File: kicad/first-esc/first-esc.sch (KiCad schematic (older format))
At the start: 0 parts

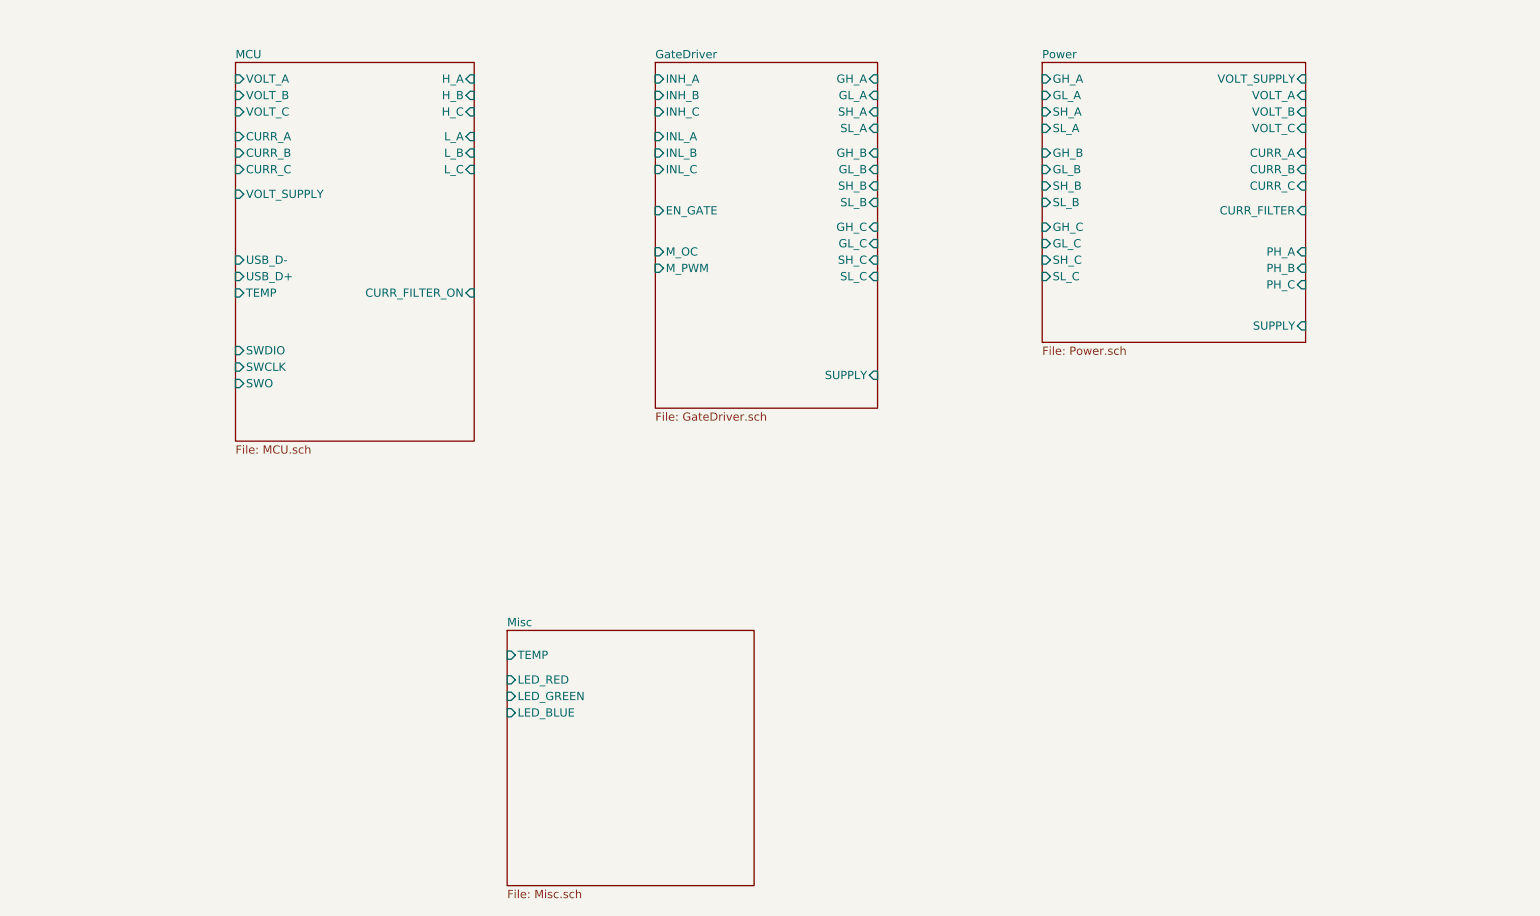
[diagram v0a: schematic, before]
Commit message: (hopefully) finishing up PCB schematic
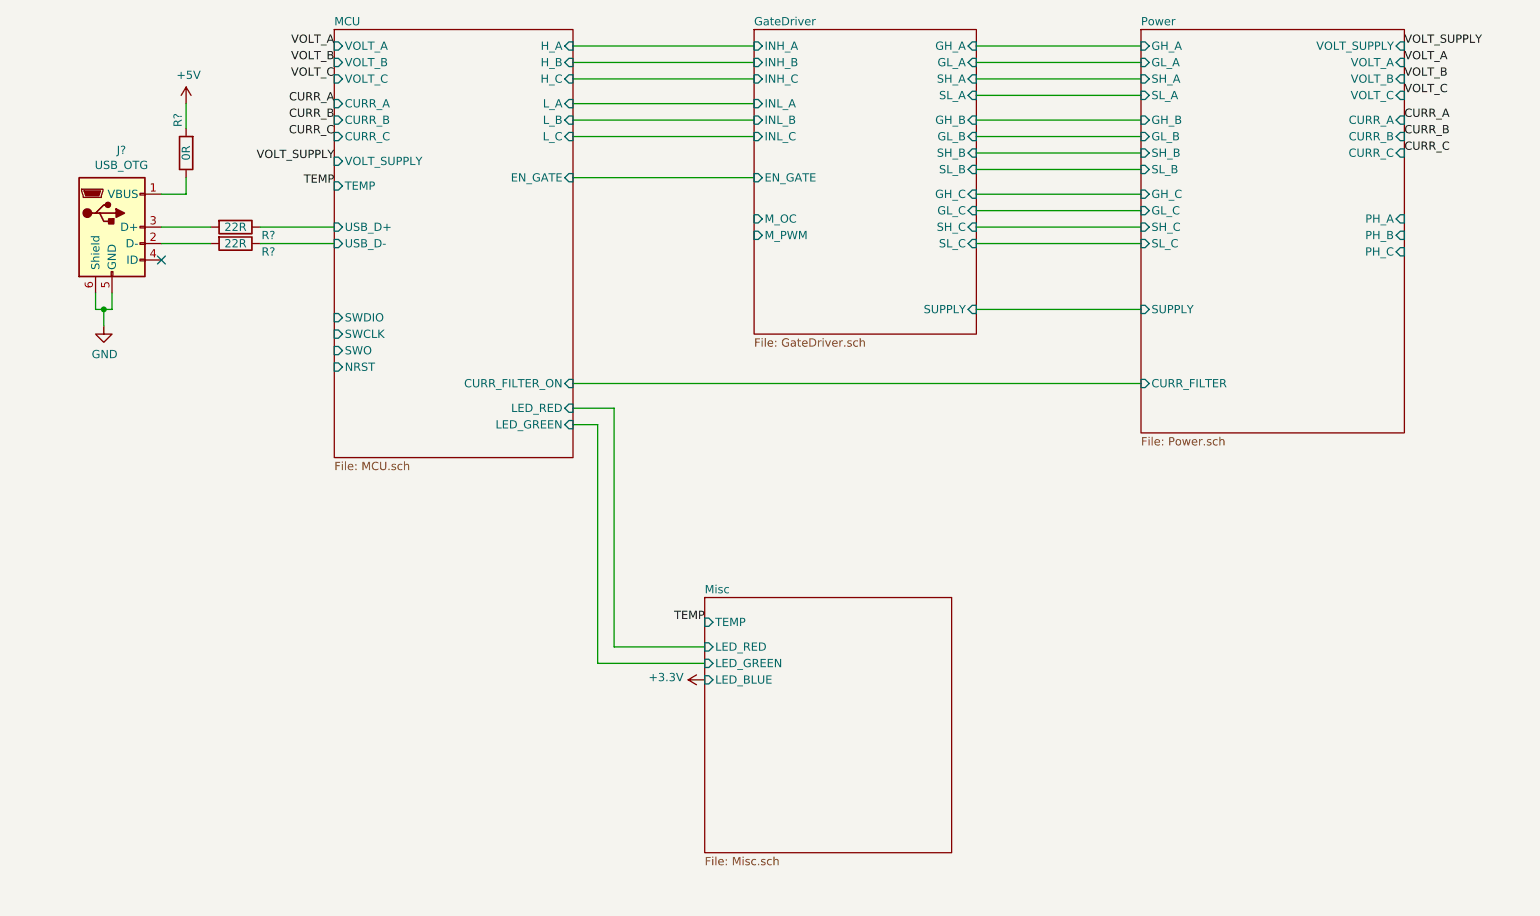
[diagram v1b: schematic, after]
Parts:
- added J?: USB_OTG, symbol Connector:USB_OTG
- added R? (x2): 22R, symbol Device:R
- added R?: 0R, symbol Device:R
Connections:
- net MCU/USB_D+: now also R?.1
- net MCU/USB_D-: now also R?.1
- new net: J?.1 (VBUS), R?.1
- new net: J?.2 (D-), R?.2
- new net: J?.3 (D+), R?.2
- new net +5V: R?.2
- new net GND: J?.5 (GND), J?.6 (Shield)
- no-connect marks 0 -> 1

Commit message: mostly finished schematic, started PCB layout
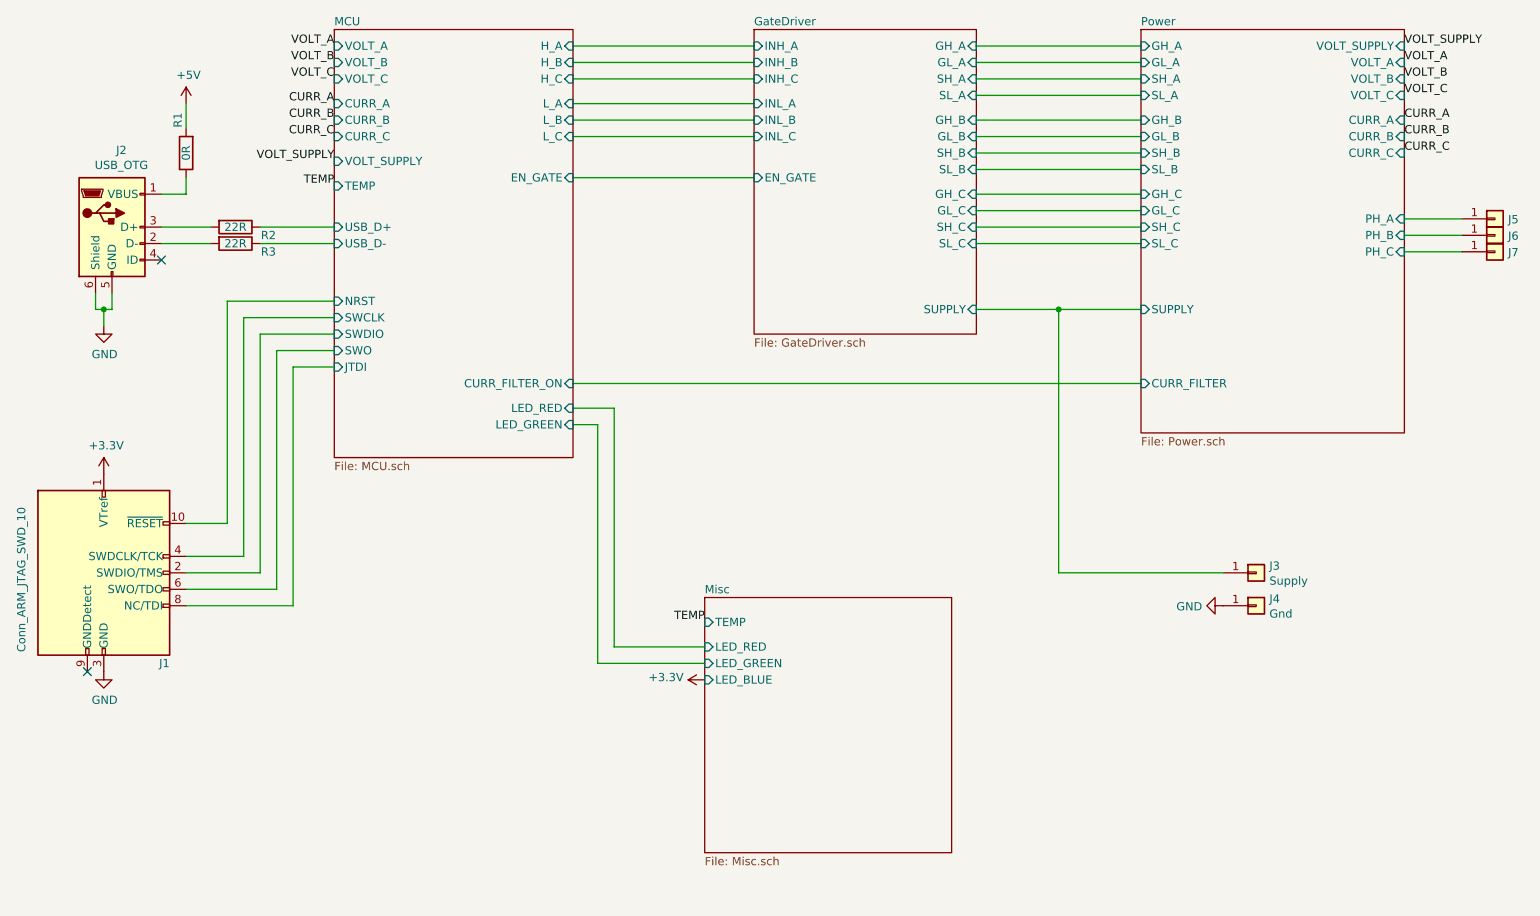
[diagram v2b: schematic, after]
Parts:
- added J1: Conn_ARM_JTAG_SWD_10, Connector_PinHeader_1.27mm:PinHeader_2x05_P1.27mm_Vertical, symbol Connector:Conn_ARM_JTAG_SWD_10
- added J3: Supply, Connector_Wire:SolderWirePad_1x01_SMD_5x10mm, symbol Connector_Generic:Conn_01x01
- added J4: Gnd, Connector_Wire:SolderWirePad_1x01_SMD_5x10mm, symbol Connector_Generic:Conn_01x01
- added J5: PH_A, Connector_Wire:SolderWirePad_1x01_SMD_5x10mm, symbol Connector_Generic:Conn_01x01
- added J6: PH_B, Connector_Wire:SolderWirePad_1x01_SMD_5x10mm, symbol Connector_Generic:Conn_01x01
- added J7: PH_C, Connector_Wire:SolderWirePad_1x01_SMD_5x10mm, symbol Connector_Generic:Conn_01x01
- J2: renamed from J?; footprint (none) -> Connector_USB:USB_Micro-B_Molex-105017-0001
- R1, R2, R3: renamed from R?; footprint (none) -> Resistor_SMD:R_0603_1608Metric
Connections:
- net +3V3: now also J1.1 (VTref)
- net GND: now also J1.3 (GND), J1.5 (GND), J4.1 (Pin_1)
- net GateDriver/SUPPLY: now also J3.1 (Pin_1)
- net MCU/NRST: now also J1.10 (~RESET~)
- net MCU/SWCLK: now also J1.4 (SWDCLK/TCK)
- net MCU/SWDIO: now also J1.2 (SWDIO/TMS)
- net MCU/SWO: now also J1.6 (SWO/TDO)
- net Power/PH_A: now also J5.1 (Pin_1)
- net Power/PH_B: now also J6.1 (Pin_1)
- net Power/PH_C: now also J7.1 (Pin_1)
- new net MCU/JTDI: J1.8 (NC/TDI)
- no-connect marks 1 -> 2
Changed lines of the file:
@@
 F19 "INL_C" I L 5450 2300 50
 F20 "EN_GATE" I L 5450 2550 50
-F21 "M_OC" I L 5450 2800 50
-F22 "M_PWM" I L 5450 2900 50
-F23 "SUPPLY" I R 6800 3350 50
+F21 "SUPPLY" I R 6800 3350 50
 $EndSheet
 $Sheet
@@
 $EndSheet
 $Comp
-L power:+3.3V #PWR?
+L power:+3.3V #PWR0101
 U 1 1 600E73DD
 P 5150 5600
-F 0 "#PWR?" H 5150 5450 50  0001 C CNN
+F 0 "#PWR0101" H 5150 5450 50  0001 C CNN
 F 1 "+3.3V" V 5165 5728 50  0000 L CNN
 F 2 "" H 5150 5600 50  0001 C CNN
@@
 F17 "VOLT_SUPPLY" I L 2900 2450 50
 F18 "CURR_FILTER_ON" I R 4350 3800 50
-F19 "SWDIO" I L 2900 3400 50
-F20 "SWCLK" I L 2900 3500 50
+F19 "SWDIO" I L 2900 3500 50
+F20 "SWCLK" I L 2900 3400 50
 F21 "SWO" I L 2900 3600 50
-F22 "NRST" I L 2900 3700 50
+F22 "NRST" I L 2900 3300 50
 F23 "EN_GATE" I R 4350 2550 50
 F24 "LED_GREEN" I R 4350 4050 50
 F25 "LED_RED" I R 4350 3950 50
+F26 "JTDI" I L 2900 3700 50
 $EndSheet
 Wire Wire Line
@@
 	6800 2950 7800 2950
 Wire Wire Line
-	6800 3350 7800 3350
+	6800 3350 7300 3350
 Text Label 9400 1750 0    50   ~ 0
 VOLT_SUPPLY
@@
 TEMP
 $Comp
-L Connector:USB_OTG J?
+L Connector:USB_OTG J2
 U 1 1 600ED622
 P 1550 2850
-F 0 "J?" H 1607 3317 50  0000 C CNN
+F 0 "J2" H 1607 3317 50  0000 C CNN
 F 1 "USB_OTG" H 1607 3226 50  0000 C CNN
-F 2 "" H 1700 2800 50  0001 C CNN
+F 2 "Connector_USB:USB_Micro-B_Molex-105017-0001" H 1700 2800 50  0001 C CNN
 F 3 " ~" H 1700 2800 50  0001 C CNN
 	1    1550 2850
@@
 	1550 3350 1550 3250
 $Comp
-L power:GND #PWR?
+L power:GND #PWR0102
 U 1 1 600F02F2
 P 1500 3450
-F 0 "#PWR?" H 1500 3200 50  0001 C CNN
+F 0 "#PWR0102" H 1500 3200 50  0001 C CNN
 F 1 "GND" H 1505 3277 50  0000 C CNN
 F 2 "" H 1500 3450 50  0001 C CNN
@@
 	1500 3350 1550 3350
 $Comp
-L Device:R R?
+L Device:R R2
 U 1 1 600F1189
 P 2300 2850
-F 0 "R?" V 2350 3050 50  0000 C CNN
+F 0 "R2" V 2350 3050 50  0000 C CNN
 F 1 "22R" V 2300 2850 50  0000 C CNN
-F 2 "" V 2230 2850 50  0001 C CNN
+F 2 "Resistor_SMD:R_0603_1608Metric" V 2230 2850 50  0001 C CNN
 F 3 "~" H 2300 2850 50  0001 C CNN
 	1    2300 2850
@@
 $EndComp
 $Comp
-L Device:R R?
+L Device:R R3
 U 1 1 600F17F0
 P 2300 2950
-F 0 "R?" V 2350 3150 50  0000 C CNN
+F 0 "R3" V 2350 3150 50  0000 C CNN
 F 1 "22R" V 2300 2950 50  0000 C CNN
-F 2 "" V 2230 2950 50  0001 C CNN
+F 2 "Resistor_SMD:R_0603_1608Metric" V 2230 2950 50  0001 C CNN
 F 3 "~" H 2300 2950 50  0001 C CNN
 	1    2300 2950
@@
 NoConn ~ 1850 3050
 $Comp
-L Device:R R?
+L Device:R R1
 U 1 1 600F4DDD
 P 2000 2400
-F 0 "R?" V 2050 2200 50  0000 C CNN
+F 0 "R1" V 2050 2200 50  0000 C CNN
 F 1 "0R" V 2000 2400 50  0000 C CNN
-F 2 "" V 1930 2400 50  0001 C CNN
+F 2 "Resistor_SMD:R_0603_1608Metric" V 1930 2400 50  0001 C CNN
 F 3 "~" H 2000 2400 50  0001 C CNN
 	1    2000 2400
@@
 $EndComp
 $Comp
-L power:+5V #PWR?
+L power:+5V #PWR0103
 U 1 1 600F5166
 P 2000 2100
-F 0 "#PWR?" H 2000 1950 50  0001 C CNN
+F 0 "#PWR0103" H 2000 1950 50  0001 C CNN
 F 1 "+5V" H 2015 2273 50  0000 C CNN
 F 2 "" H 2000 2100 50  0001 C CNN
@@
 Wire Wire Line
 	2000 2100 2000 2250
+$Comp
+L Connector:Conn_ARM_JTAG_SWD_10 J1
+U 1 1 600FCC9D
+P 1500 4950
+F 0 "J1" H 1900 4400 50  0000 R CNN
+F 1 "Conn_ARM_JTAG_SWD_10" V 1000 5350 50  0000 R CNN
+F 2 "Connector_PinHeader_1.27mm:PinHeader_2x05_P1.27mm_Vertical" H 1500 4950 50  0001 C CNN
+F 3 "http://infocenter.arm.com/help/topic/com.arm.doc.ddi0314h/DDI0314H_coresight_components_trm.pdf" V 1150 3700 50  0001 C CNN
+	1    1500 4950
+	1    0    0    -1
+$EndComp
+Wire Wire Line
+	2900 3300 2250 3300
+Wire Wire Line
+	2250 3300 2250 4650
+Wire Wire Line
+	2250 4650 2000 4650
+Wire Wire Line
+	2900 3400 2350 3400
+Wire Wire Line
+	2350 3400 2350 4850
+Wire Wire Line
+	2350 4850 2000 4850
+Wire Wire Line
+	2900 3500 2450 3500
+Wire Wire Line
+	2450 3500 2450 4950
+Wire Wire Line
+	2450 4950 2000 4950
+Wire Wire Line
+	2900 3600 2550 3600
+Wire Wire Line
+	2550 3600 2550 5050
+Wire Wire Line
+	2550 5050 2000 5050
+$Comp
+L power:+3.3V #PWR0104
+U 1 1 60102BF9
+P 1500 4350
+F 0 "#PWR0104" H 1500 4200 50  0001 C CNN
+F 1 "+3.3V" H 1515 4523 50  0000 C CNN
+F 2 "" H 1500 4350 50  0001 C CNN
+F 3 "" H 1500 4350 50  0001 C CNN
+	1    1500 4350
+	1    0    0    -1
+$EndComp
+Wire Wire Line
+	2900 3700 2650 3700
+Wire Wire Line
+	2650 3700 2650 5150
+Wire Wire Line
+	2650 5150 2000 5150
+$Comp
+L power:GND #PWR0105
+U 1 1 601066CB
+P 1500 5550
+F 0 "#PWR0105" H 1500 5300 50  0001 C CNN
+F 1 "GND" H 1505 5377 50  0000 C CNN
+F 2 "" H 1500 5550 50  0001 C CNN
+F 3 "" H 1500 5550 50  0001 C CNN
+	1    1500 5550
+	1    0    0    -1
+$EndComp
+NoConn ~ 1400 5550
+$Comp
+L Connector_Generic:Conn_01x01 J5
+U 1 1 60108A0B
+P 9950 2800
+F 0 "J5" H 10030 2796 50  0000 L CNN
+F 1 "PH_A" H 10030 2751 50  0001 L CNN
+F 2 "Connector_Wire:SolderWirePad_1x01_SMD_5x10mm" H 9950 2800 50  0001 C CNN
+F 3 "~" H 9950 2800 50  0001 C CNN
+	1    9950 2800
+	1    0    0    -1
+$EndComp
+$Comp
+L Connector_Generic:Conn_01x01 J6
+U 1 1 60109269
+P 9950 2900
+F 0 "J6" H 10030 2896 50  0000 L CNN
+F 1 "PH_B" H 10030 2851 50  0001 L CNN
+F 2 "Connector_Wire:SolderWirePad_1x01_SMD_5x10mm" H 9950 2900 50  0001 C CNN
+F 3 "~" H 9950 2900 50  0001 C CNN
+	1    9950 2900
+	1    0    0    -1
+$EndComp
+$Comp
+L Connector_Generic:Conn_01x01 J7
+U 1 1 60109510
+P 9950 3000
+F 0 "J7" H 10030 2996 50  0000 L CNN
+F 1 "PH_C" H 10030 2951 50  0001 L CNN
+F 2 "Connector_Wire:SolderWirePad_1x01_SMD_5x10mm" H 9950 3000 50  0001 C CNN
+F 3 "~" H 9950 3000 50  0001 C CNN
+	1    9950 3000
+	1    0    0    -1
+$EndComp
+Wire Wire Line
+	9400 2800 9750 2800
+Wire Wire Line
+	9750 2900 9400 2900
+Wire Wire Line
+	9400 3000 9750 3000
+$Comp
+L Connector_Generic:Conn_01x01 J3
+U 1 1 6010DF51
+P 8500 4950
+F 0 "J3" H 8580 4992 50  0000 L CNN
+F 1 "Supply" H 8580 4901 50  0000 L CNN
+F 2 "Connector_Wire:SolderWirePad_1x01_SMD_5x10mm" H 8500 4950 50  0001 C CNN
+F 3 "~" H 8500 4950 50  0001 C CNN
+	1    8500 4950
+	1    0    0    -1
+$EndComp
+$Comp
+L Connector_Generic:Conn_01x01 J4
+U 1 1 6010E5B3
+P 8500 5150
+F 0 "J4" H 8580 5192 50  0000 L CNN
+F 1 "Gnd" H 8580 5101 50  0000 L CNN
+F 2 "Connector_Wire:SolderWirePad_1x01_SMD_5x10mm" H 8500 5150 50  0001 C CNN
+F 3 "~" H 8500 5150 50  0001 C CNN
+	1    8500 5150
+	1    0    0    -1
+$EndComp
+$Comp
+L power:GND #PWR0106
+U 1 1 6010E94F
+P 8300 5150
+F 0 "#PWR0106" H 8300 4900 50  0001 C CNN
+F 1 "GND" V 8305 5022 50  0000 R CNN
+F 2 "" H 8300 5150 50  0001 C CNN
+F 3 "" H 8300 5150 50  0001 C CNN
+	1    8300 5150
+	0    1    1    0
+$EndComp
+Wire Wire Line
+	7300 3350 7300 4950
+Wire Wire Line
+	7300 4950 8300 4950
+Connection ~ 7300 3350
+Wire Wire Line
+	7300 3350 7800 3350
 $EndSCHEMATC
